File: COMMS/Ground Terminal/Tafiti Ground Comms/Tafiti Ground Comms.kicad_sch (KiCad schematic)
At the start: 64 parts

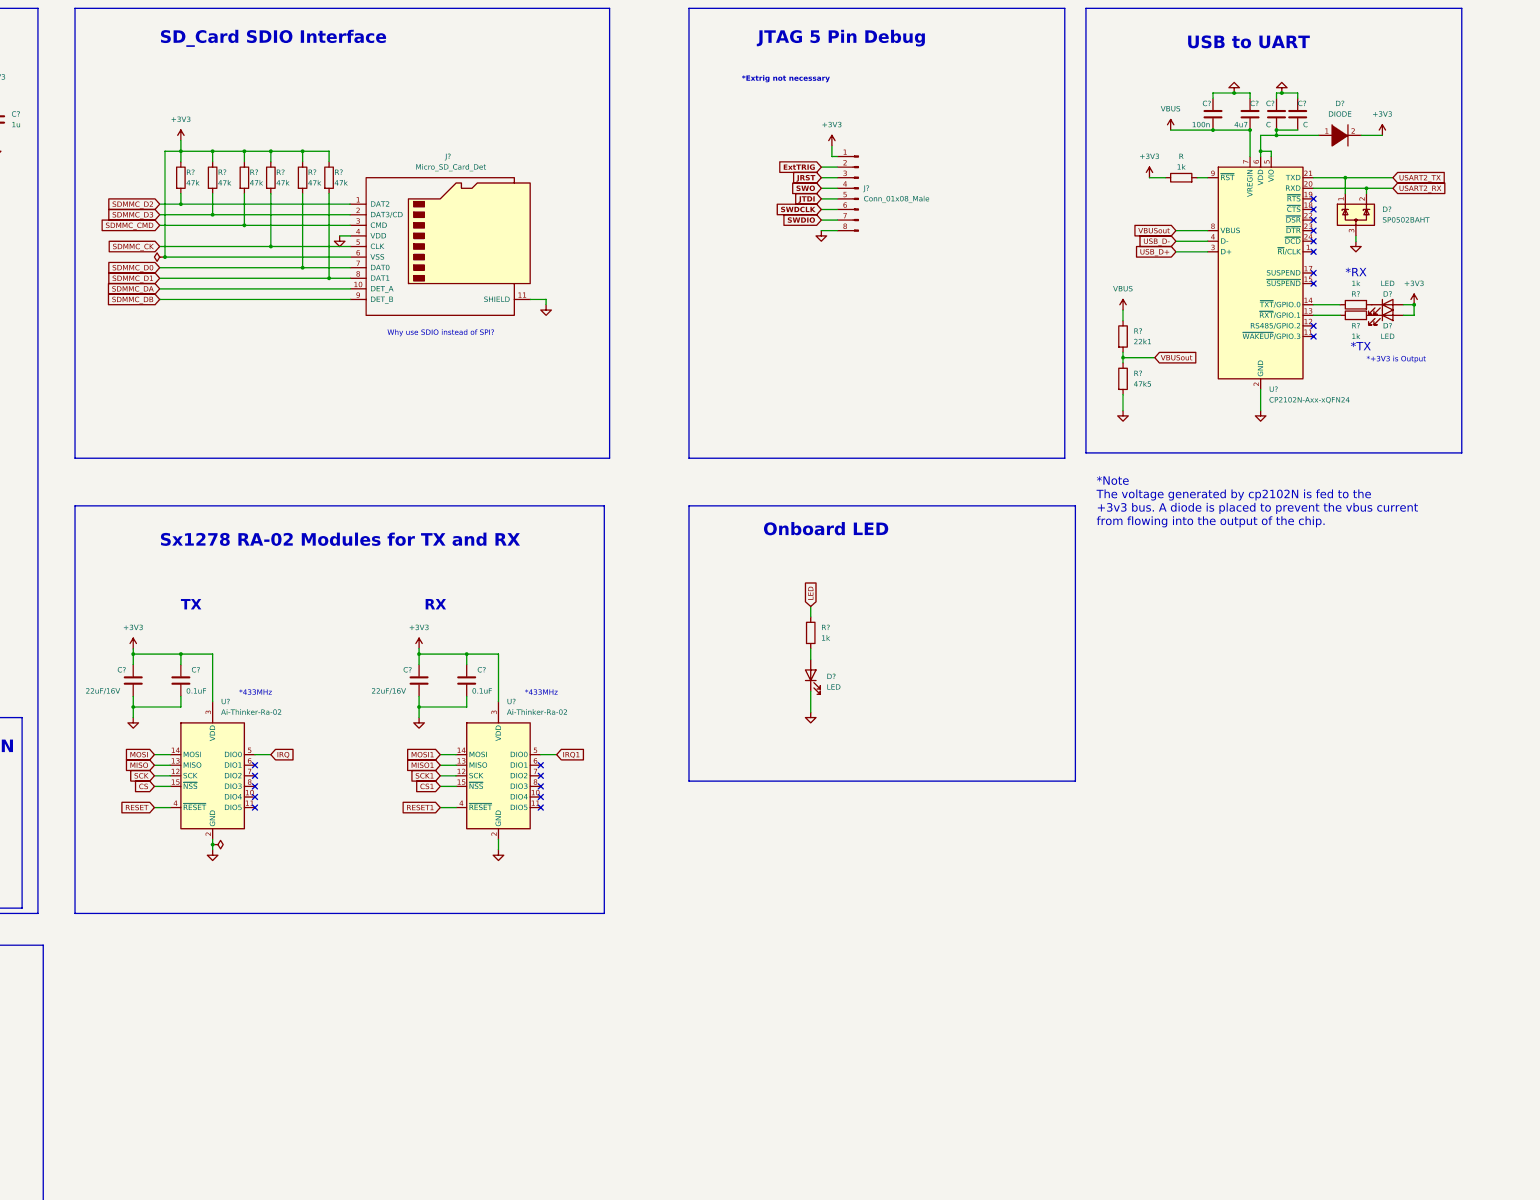
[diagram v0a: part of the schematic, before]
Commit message: Added Ground Terminal files
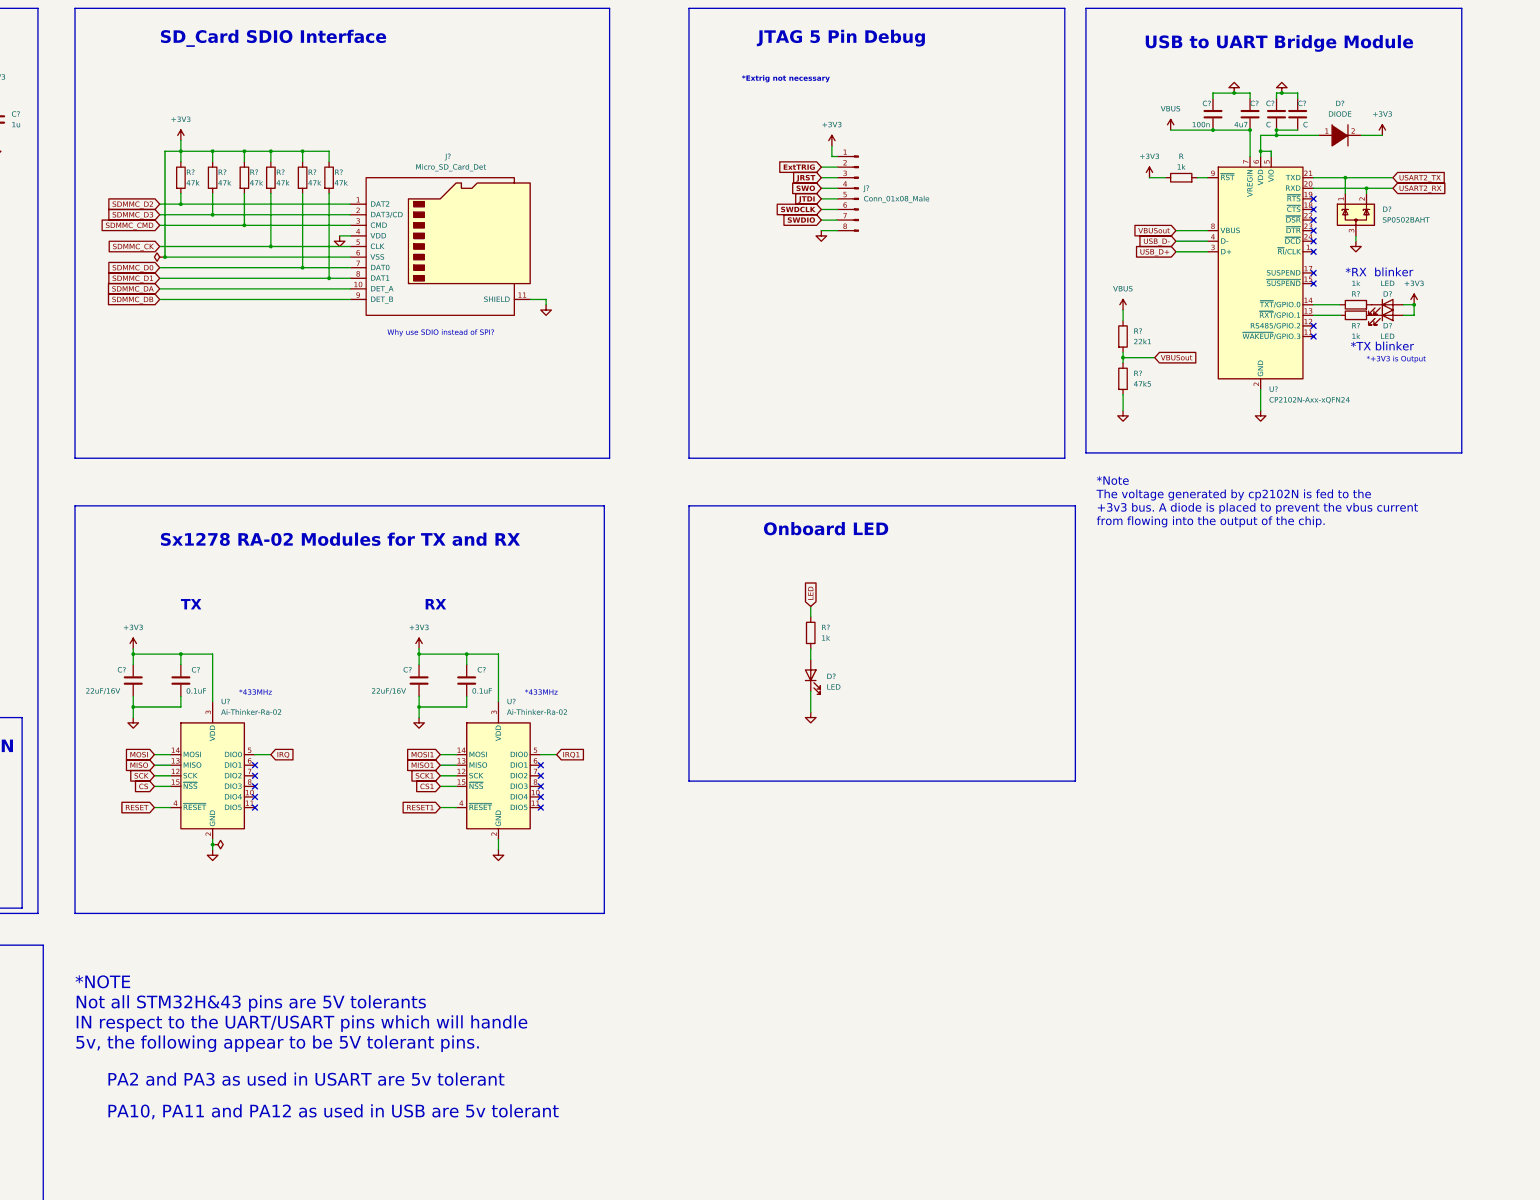
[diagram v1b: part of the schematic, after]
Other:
- note added: "*NOTE Not all STM32H&43 pins are 5V tolerants IN respect to the UART/USART pins which will handle 5v, the following appear to be 5V tolerant pins."
- note added: "*RX blinker"
- note added: "*TX blinker"
- note added: "PA10, PA11 and PA12 as used in USB are 5v tolerant"
- note added: "PA2 and PA3 as used in USART are 5v tolerant"
- note added: "USB to UART Bridge Module"
- note removed: "*RX"
- note removed: "*TX"
- note removed: "USB to UART"
- company: Kenya Space Agency -> For Kenya Space Agency by Gerald Mbuthia
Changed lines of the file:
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@@
     (date "2023-03-05")
     (rev "V1.4")
-    (company "Kenya Space Agency")
+    (company "For Kenya Space Agency by Gerald Mbuthia")
     (comment 1 "This is a portable ground receiver module to send  and receive signals from the Onboard comms of Tafiti Nano-satellite.")
   )
@@
     (effects (font (size 1.27 1.27)) (justify left bottom))
   )
-  (text "*RX" (at 549.91 100.33 0)
+  (text "*RX  blinker" (at 549.91 100.33 0)
     (effects (font (size 2 2)) (justify left bottom))
+  )
+  (text "PA2 and PA3 as used in USART are 5v tolerant" (at 252.73 294.64 0)
+    (effects (font (size 3 3)) (justify left bottom))
   )
   (text "*UART\n*USB" (at 34.29 377.19 0)
@@
     (effects (font (size 1.27 1.27)) (justify left bottom))
   )
+  (text "PA10, PA11 and PA12 as used in USB are 5v tolerant"
+    (at 252.73 302.26 0)
+    (effects (font (size 3 3)) (justify left bottom))
+  )
   (text "Why use SDIO instead of SPI?\n" (at 320.04 114.3 0)
     (effects (font (size 1.27 1.27)) (justify left bottom))
@@
     (effects (font (size 2 2) bold) (justify left bottom))
   )
-  (text "USB to UART " (at 511.81 45.72 0)
+  (text "USB to UART Bridge Module" (at 501.65 45.72 0)
     (effects (font (size 3 3) bold) (justify left bottom))
   )
@@
   (text "*433MHz" (at 284.48 200.66 0)
     (effects (font (size 1.27 1.27)) (justify left bottom))
+  )
+  (text "*NOTE\nNot all STM32H&43 pins are 5V tolerants\nIN respect to the UART/USART pins which will handle \n5v, the following appear to be 5V tolerant pins.\n"
+    (at 245.11 285.75 0)
+    (effects (font (size 3 3)) (justify left bottom))
   )
   (text "Low Speed Clock" (at 38.1 209.55 0)
@@
     (effects (font (size 2.5 2.5) bold) (justify left bottom))
   )
-  (text "*TX" (at 551.18 118.11 0)
+  (text "*TX blinker" (at 551.18 118.11 0)
     (effects (font (size 2 2)) (justify left bottom))
   )

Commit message: Added the Tafiti Ground Terminal
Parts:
- 1k1: renamed from 1k; footprint (none) -> Resistor_SMD:R_0402_1005Metric
- C14, C18, C24, C25: renamed from C?; footprint (none) -> Capacitor_SMD:C_0603_1608Metric
- C26: renamed from C?; value C -> 4u7; footprint (none) -> Capacitor_SMD:C_0603_1608Metric
- C27: renamed from C?; value C -> 100n; footprint (none) -> Capacitor_SMD:C_0603_1608Metric
- D5: renamed from D?; footprint (none) -> Diode_SMD:D_0603_1608Metric
- D7, D8: renamed from D?; footprint (none) -> LED_SMD:LED_0603_1608Metric
- J1, J2: renamed from J?; footprint (none) -> Connector_USB:USB_Micro-B_Wuerth_629105150521
- R11, R12: renamed from R?; footprint (none) -> Resistor_SMD:R_0603_1608Metric
- R13, R14: renamed from R?; footprint (none) -> Resistor_SMD:R_0402_1005Metric
- gave numbers to parts that had none: 48
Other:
- note added: "*Confirm values for capacitors c26 and c27"
- note added: "NOTE Change the ESD protection diodes into those of similar values to reduce costs and complexities"

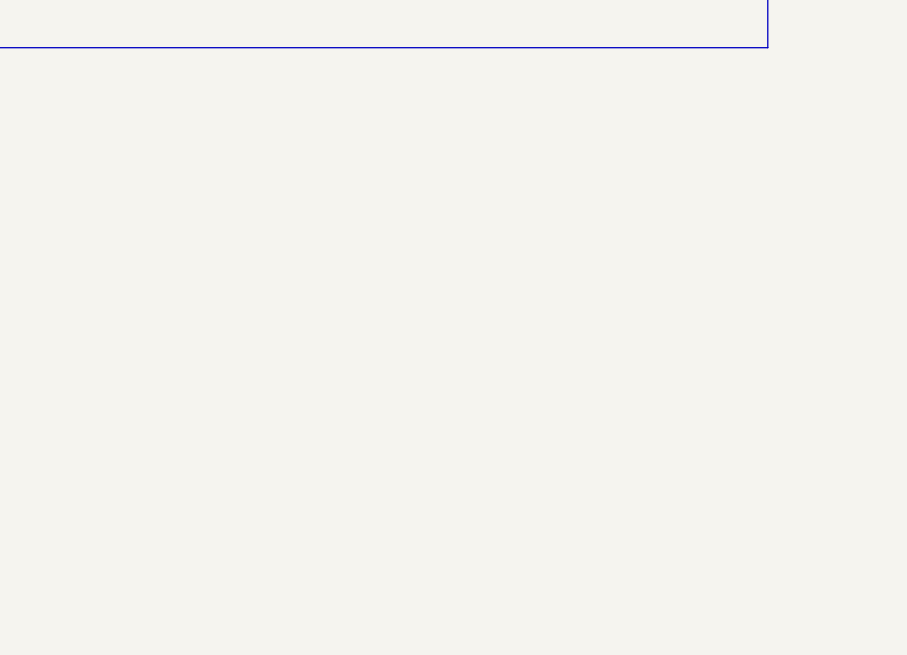
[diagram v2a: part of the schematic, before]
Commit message: Made minor changes to add mounting holes
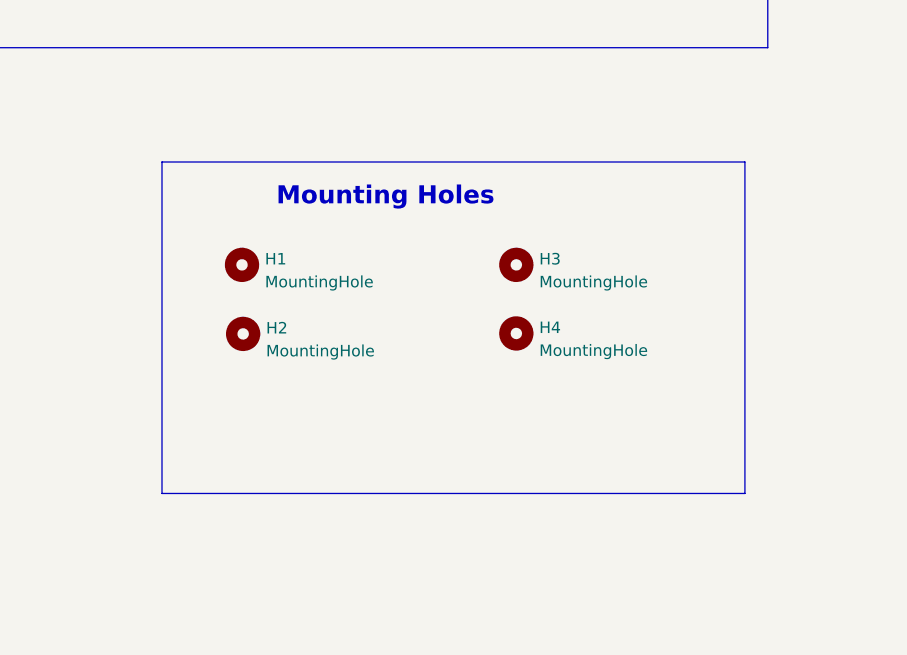
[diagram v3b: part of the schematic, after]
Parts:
- added H1, H2, H3, H4: MountingHole, MountingHole:MountingHole_3.2mm_M3, symbol Mechanical:MountingHole
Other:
- note added: "Mounting Holes"
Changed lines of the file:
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@@
     (stroke (width 0) (type default))
   )
+  (polyline (pts (xy 482.6 270.51) (xy 417.83 270.51))
+    (stroke (width 0) (type default))
+  )
   (wire (pts (xy 119.38 298.45) (xy 130.81 298.45))
     (stroke (width 0) (type default))
@@
     (stroke (width 0) (type default))
   )
+  (polyline (pts (xy 417.83 233.68) (xy 482.6 233.68))
+    (stroke (width 0) (type default))
+  )
   (wire (pts (xy 153.67 213.36) (xy 156.21 213.36))
     (stroke (width 0) (type default))
@@
     (stroke (width 0) (type default))
   )
+  (polyline (pts (xy 482.6 233.68) (xy 482.6 270.51))
+    (stroke (width 0) (type default))
+  )
   (polyline (pts (xy 29.21 142.24) (xy 97.79 142.24))
     (stroke (width 0) (type default))
@@
     (stroke (width 0) (type default))
   )
+  (polyline (pts (xy 417.83 233.68) (xy 417.83 270.51))
+    (stroke (width 0) (type default))
+  )
   (polyline (pts (xy 187.96 251.46) (xy 187.96 205.74))
     (stroke (width 0) (type default))
@@
     (effects (font (size 3 3) bold) (justify left bottom))
   )
+  (text "Mounting Holes" (at 430.53 238.76 0)
+    (effects (font (size 2 2) (thickness 0.4) bold) (justify left bottom))
+  )
   (text "*Note\nThe voltage generated by cp2102N is fed to the \n+3v3 bus. A diode is placed to prevent the vbus current \nfrom flowing into the output of the chip."
     (at 490.22 160.02 0)
@@
     )
   )
+  (symbol (lib_id "Mechanical:MountingHole") (at 426.8464 252.7811 0) (unit 1)
+    (in_bom yes) (on_board yes) (dnp no) (fields_autoplaced)
+    (property "Reference" "H2" (at 429.3864 252.1461 0)
+      (effects (font (size 1.27 1.27)) (justify left))
+    )
+    (property "Value" "MountingHole" (at 429.3864 254.6861 0)
+      (effects (font (size 1.27 1.27)) (justify left))
+    )
+    (property "Footprint" "MountingHole:MountingHole_3.2mm_M3" (at 426.8464 252.7811 0)
+      (effects (font (size 1.27 1.27)) hide)
+    )
+    (property "Datasheet" "~" (at 426.8464 252.7811 0)
+      (effects (font (size 1.27 1.27)) hide)
+    )
+    (instances
+      (project "Tafiti Ground Comms"
+        (path "/3ef6b452-cc77-4564-bfd4-11d6e32ad6f7"
+          (reference "H2") (unit 1)
+        )
+      )
+    )
+  )
   (symbol (lib_id "Device:R") (at 130.81 93.98 90) (unit 1)
     (in_bom yes) (on_board yes) (dnp no)
@@
     )
   )
+  (symbol (lib_id "Mechanical:MountingHole") (at 457.2 252.73 0) (unit 1)
+    (in_bom yes) (on_board yes) (dnp no) (fields_autoplaced)
+    (property "Reference" "H4" (at 459.74 252.095 0)
+      (effects (font (size 1.27 1.27)) (justify left))
+    )
+    (property "Value" "MountingHole" (at 459.74 254.635 0)
+      (effects (font (size 1.27 1.27)) (justify left))
+    )
+    (property "Footprint" "MountingHole:MountingHole_3.2mm_M3" (at 457.2 252.73 0)
+      (effects (font (size 1.27 1.27)) hide)
+    )
+    (property "Datasheet" "~" (at 457.2 252.73 0)
+      (effects (font (size 1.27 1.27)) hide)
+    )
+    (instances
+      (project "Tafiti Ground Comms"
+        (path "/3ef6b452-cc77-4564-bfd4-11d6e32ad6f7"
+          (reference "H4") (unit 1)
+        )
+      )
+    )
+  )
   (symbol (lib_id "power:+3V3") (at 153.67 57.15 0) (unit 1)
     (in_bom yes) (on_board yes) (dnp no) (fields_autoplaced)
@@
     )
   )
+  (symbol (lib_id "Mechanical:MountingHole") (at 457.2 245.11 0) (unit 1)
+    (in_bom yes) (on_board yes) (dnp no) (fields_autoplaced)
+    (property "Reference" "H3" (at 459.74 244.475 0)
+      (effects (font (size 1.27 1.27)) (justify left))
+    )
+    (property "Value" "MountingHole" (at 459.74 247.015 0)
+      (effects (font (size 1.27 1.27)) (justify left))
+    )
+    (property "Footprint" "MountingHole:MountingHole_3.2mm_M3" (at 457.2 245.11 0)
+      (effects (font (size 1.27 1.27)) hide)
+    )
+    (property "Datasheet" "~" (at 457.2 245.11 0)
+      (effects (font (size 1.27 1.27)) hide)
+    )
+    (instances
+      (project "Tafiti Ground Comms"
+        (path "/3ef6b452-cc77-4564-bfd4-11d6e32ad6f7"
+          (reference "H3") (unit 1)
+        )
+      )
+    )
+  )
   (symbol (lib_id "power:GND") (at 278.13 237.49 0) (unit 1)
     (in_bom yes) (on_board yes) (dnp no) (fields_autoplaced)
@@
         )
       )
+    )
+  )
+  (symbol (lib_id "Mechanical:MountingHole") (at 426.72 245.11 0) (unit 1)
+    (in_bom yes) (on_board yes) (dnp no) (fields_autoplaced)
+    (property "Reference" "H1" (at 429.26 244.475 0)
+      (effects (font (size 1.27 1.27)) (justify left))
+    )
+    (property "Value" "MountingHole" (at 429.26 247.015 0)
+      (effects (font (size 1.27 1.27)) (justify left))
+    )
+    (property "Footprint" "MountingHole:MountingHole_3.2mm_M3" (at 426.72 245.11 0)
+      (effects (font (size 1.27 1.27)) hide)
+    )
+    (property "Datasheet" "~" (at 426.72 245.11 0)
+      (effects (font (size 1.27 1.27)) hide)
+    )
+    (instances
+      (project "Tafiti Ground Comms"
+        (path "/3ef6b452-cc77-4564-bfd4-11d6e32ad6f7"
+          (reference "H1") (unit 1)
+        )
+      )
